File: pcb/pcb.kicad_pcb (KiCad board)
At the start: 2 copper layers, 1 part

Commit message: Finalisation PCB
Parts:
- removed REF**: MODULE_NUCLEO-L432KC, NUCLEO-L432KC:MODULE_NUCLEO-L432KC
- added C1: 1n, Capacitor_THT:CP_Radial_D4.0mm_P1.50mm, F.Cu at (114.3, 119.4)
- added C2: 10u, Capacitor_THT:CP_Radial_D4.0mm_P1.50mm, F.Cu at (74.0, 119.0)
- added C3: 1u, Capacitor_THT:CP_Radial_D4.0mm_P1.50mm, F.Cu at (103.0, 103.0)
- added J1: VIN VBAT, Connector_PinHeader_2.00mm:PinHeader_1x04_P2.00mm_Vertical, F.Cu at (86.0, 80.0)
- added J2: Conn_01x04, Connector_PinHeader_2.00mm:PinHeader_1x04_P2.00mm_Vertical, F.Cu at (59.7, 104.7)
- added J3: AudioJack3, Connector_Audio:Jack_3.5mm_Ledino_KB3SPRS_Horizontal, F.Cu at (101.6, 119.4)
- added J4: Conn_01x04, Connector_PinHeader_2.00mm:PinHeader_1x04_P2.00mm_Vertical, F.Cu at (59.7, 92.7)
- added J5: HX711, Connector_PinHeader_2.00mm:PinHeader_1x04_P2.00mm_Vertical, F.Cu at (114.0, 85.0)
- added J6: Conn_01x04, Connector_PinHeader_2.00mm:PinHeader_1x04_P2.00mm_Vertical, F.Cu at (86.0, 86.0)
- added J7: Conn_01x04, Connector_PinHeader_2.00mm:PinHeader_1x04_P2.00mm_Vertical, F.Cu at (59.7, 81.3)
- added L432KC1: NUCLEO_L432KC, NUCLEO-L432KC:MODULE_NUCLEO-L432KC, F.Cu at (73.7, 85.1)
- added R1: 4.7k, Resistor_THT:R_Axial_DIN0204_L3.6mm_D1.6mm_P5.08mm_Horizontal, F.Cu at (108.0, 110.5)
- added R2: 10k, Resistor_THT:R_Axial_DIN0204_L3.6mm_D1.6mm_P5.08mm_Horizontal, F.Cu at (98.0, 108.0)
- added R3: 10k, Resistor_THT:R_Axial_DIN0204_L3.6mm_D1.6mm_P5.08mm_Horizontal, F.Cu at (101.6, 99.1)
- added U1: LM386, LM386N-4_NOPB:DIP794W45P254L959H508Q8, F.Cu at (113.0, 98.0)
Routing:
- net /+3V3: track 0.00 -> 138.9 mm
- net /+5V: track 0.00 -> 69.4 mm
- net Net-(C1-Pad1): track 0.00 -> 39.3 mm
- net /A2: track 0.00 -> 31.5 mm
- net /A0: track 0.00 -> 29.6 mm
- net Net-(L432KC1-PadNRST): track 0.00 -> 21.6 mm
- net GND: track 0.00 -> 17.3 mm
- net Net-(C1-Pad2): track 0.00 -> 14.4 mm
- net /D4: track 0.00 -> 11.2 mm
- net Net-(C3-Pad2): track 0.00 -> 7.24 mm
- net /D3: track 0.00 -> 6.47 mm
- net /D12: track 0.00 -> 6.45 mm
- net /A7: track 0.00 -> 5.12 mm
- net /A4: track 0.00 -> 4.99 mm
- added copper zone on B.Cu, net GND
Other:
- board outline added: 74 x 73 mm
- board text added: "HX711"

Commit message: Finalisation PCB
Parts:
- added J8: Conn_01x08, Connector_PinHeader_2.00mm:PinHeader_1x08_P2.00mm_Vertical, F.Cu at (122.0, 64.0)
- added R4: 2k, Resistor_THT:R_Axial_DIN0204_L3.6mm_D1.6mm_P5.08mm_Vertical, F.Cu at (153.0, 80.0)
- added R5: 1k, Resistor_THT:R_Axial_DIN0204_L3.6mm_D1.6mm_P5.08mm_Vertical, F.Cu at (148.0, 83.0)
- C1: value 1n -> 1u; footprint Capacitor_THT:CP_Radial_D4.0mm_P1.50mm -> Capacitor_THT:CP_Radial_D5.0mm_P2.00mm
- C2: footprint Capacitor_THT:CP_Radial_D4.0mm_P1.50mm -> Capacitor_THT:CP_Radial_D5.0mm_P2.00mm
- moved C2 103.4 mm to (177.0, 110.0)
- moved J1 67.1 mm to (153.0, 76.0)
- moved C1 62.0 mm to (176.3, 120.4)
- moved C3 62.0 mm to (165.0, 104.0)
- moved J2 62.0 mm to (121.7, 105.7)
- moved J3 62.0 mm to (163.6, 120.4)
- moved J4 62.0 mm to (121.7, 93.7)
- moved J5 62.0 mm to (176.0, 86.0)
- moved J6 62.0 mm to (148.0, 87.0)
- moved J7 62.0 mm to (121.7, 82.3)
- moved L432KC1 62.0 mm to (135.7, 86.1)
- moved R2 62.0 mm to (160.0, 109.0)
- moved R3 62.0 mm to (163.6, 100.1)
- moved U1 62.0 mm to (175.0, 99.0)
- moved R1 62.0 mm to (169.9, 111.5)
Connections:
- J1 pad 1: /A7 -> Net-(J1-Pad1)
- J6 pad 2: Net-(J6-Pad2) -> GND
- L432KC1 pad PA9: Net-(L432KC1-PadPA9) -> /D1
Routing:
- net /+3V3: track 138.9 -> 173.9 mm
- net /+5V: track 69.4 -> 92.3 mm
- net Net-(L432KC1-PadNRST): track 21.6 -> 0.00 mm
- net GND: track 17.3 -> 0.00 mm
- net /D1: track 0.00 -> 11.2 mm
- net Net-(J1-Pad1): track 0.00 -> 4.00 mm
- net /A7: track 5.12 -> 7.69 mm
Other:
- board size 74 x 73 mm -> 72 x 72 mm

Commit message: ...
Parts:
- R4: value 2k -> 1K
- R5: value 1k -> 2k
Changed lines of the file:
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@@
     (pad_to_mask_clearance 0)
     (aux_axis_origin 0 0)
-    (visible_elements FFFFEFFF)
+    (visible_elements FFFFE7FF)
     (pcbplotparams
       (layerselection 0x010fc_ffffffff)
@@
       (effects (font (size 1 1) (thickness 0.15)))
     )
-    (fp_text value 1k (at 2.54 1.92) (layer F.Fab)
+    (fp_text value 2k (at 2.54 1.92) (layer F.Fab)
       (effects (font (size 1 1) (thickness 0.15)))
     )
@@
       (effects (font (size 1 1) (thickness 0.15)))
     )
-    (fp_text value 2k (at 2.54 1.92) (layer F.Fab)
-      (effects (font (size 1 1) (thickness 0.15)))
-    )
+    (fp_text value 1K (at 2.54 1.92) (layer F.Fab)
+      (effects (font (size 1 1) (thickness 0.15)))
+    )

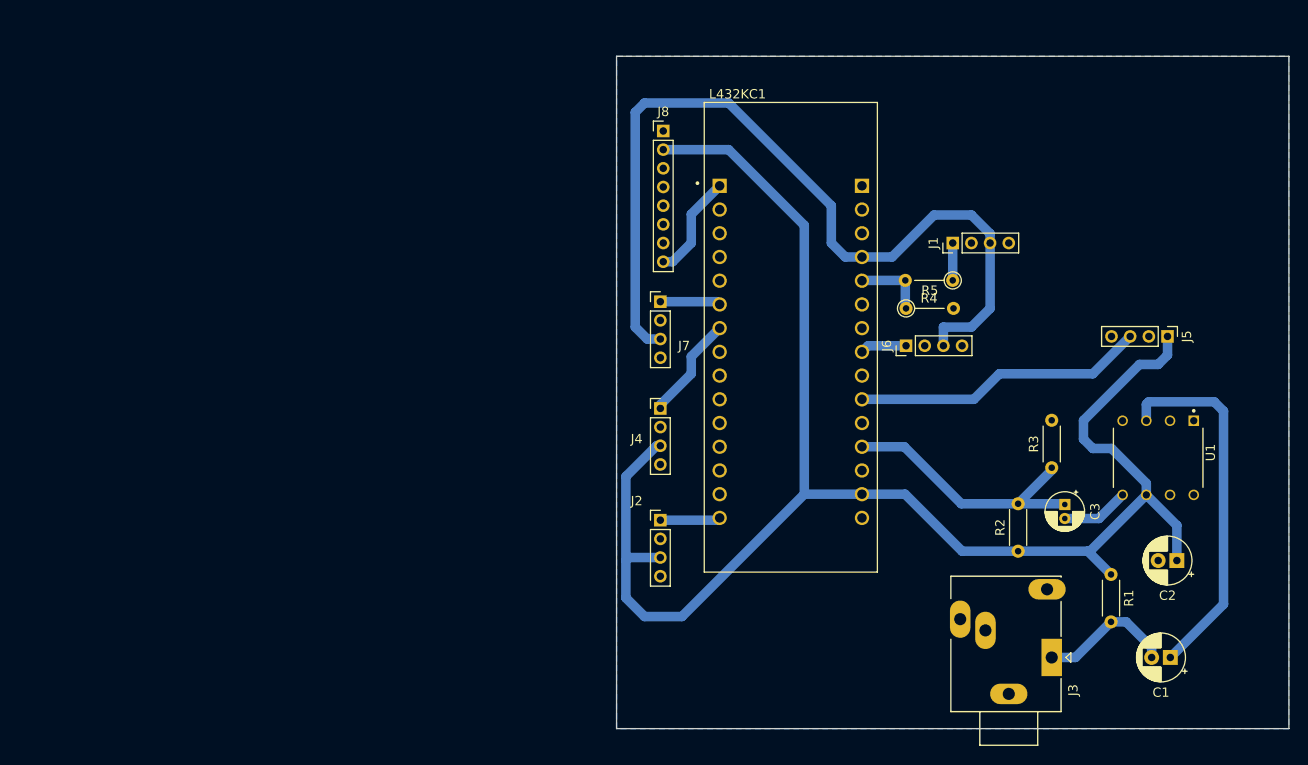
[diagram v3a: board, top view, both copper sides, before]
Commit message: Changement LDO et choix alim
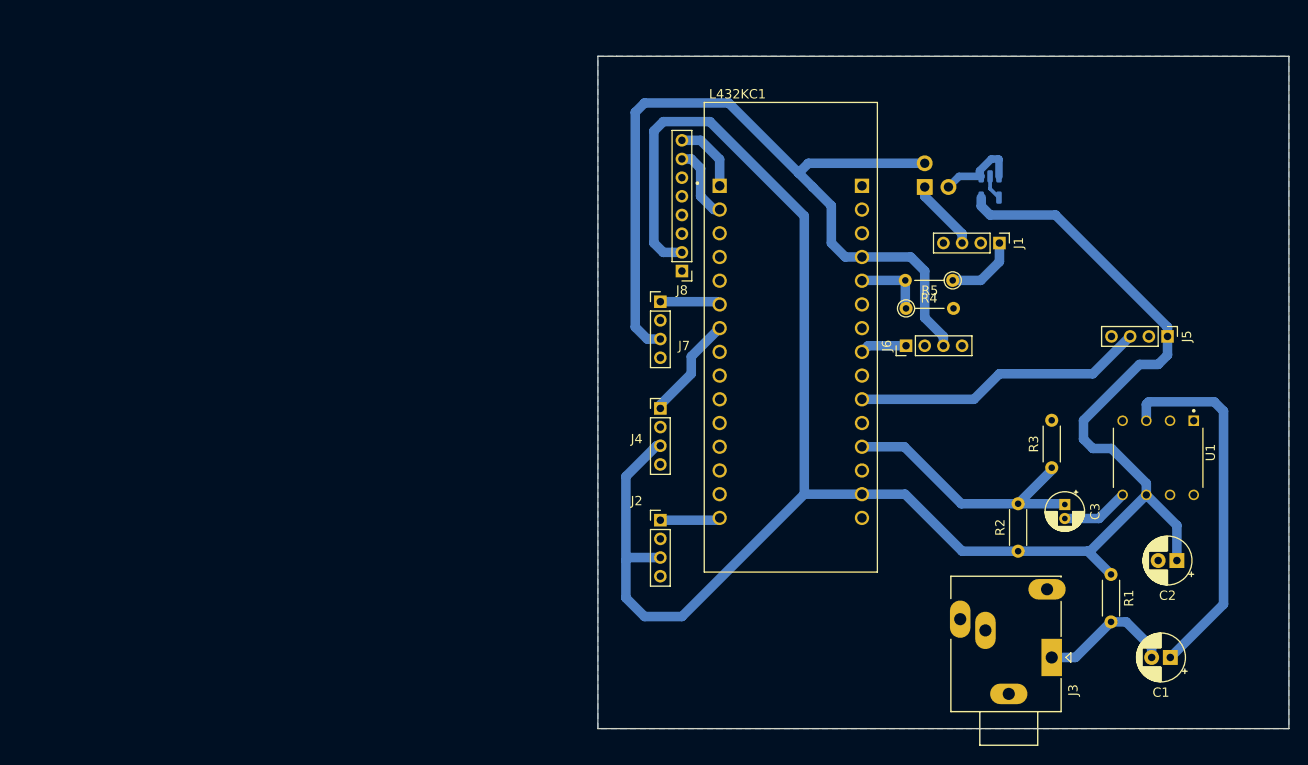
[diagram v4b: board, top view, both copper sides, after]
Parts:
- added SW1: SW_DPDT_x2, Connector_PinHeader_2.54mm:PinHeader_2x02_P2.54mm_Vertical, B.Cu at (150.0, 70.0)
- added U3: TS5205CX533, Package_TO_SOT_SMD:SOT-23-5, B.Cu at (157.0, 70.0)
- moved J8 15.1 mm to (124.0, 79.0), turned to 180 degrees
- moved J1 5.00 mm to (158.0, 76.0), turned to 270 degrees
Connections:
- J1 pad 3: /+5V -> /V_alim
- J7 pad 2: Net-(J7-Pad2) -> GND
- J8 pad 7: Net-(J8-Pad7) -> /D0
- L432KC1 pad PA10: Net-(L432KC1-PadPA10) -> /D0
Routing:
- net /+3V3: track 173.9 -> 219.8 mm
- net Net-(SW1-Pad3): track 0.00 -> 9.02 mm
- net /D0: track 0.00 -> 8.04 mm
- net /V_alim: track 0.00 -> 7.66 mm
- net Net-(J1-Pad1): track 4.00 -> 7.83 mm
- net /D1: track 11.2 -> 7.72 mm
- net GND: track 0.00 -> 2.67 mm
- net /+5V: track 92.3 -> 90.2 mm
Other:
- board size 72 x 72 mm -> 74 x 72 mm

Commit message: Finalisation PCB
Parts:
- added C4: 470p, Capacitor_SMD:C_0805_2012Metric_Pad1.18x1.45mm_HandSolder, B.Cu at (160.0, 68.0)
- added C5: 2.2u, Capacitor_SMD:C_0805_2012Metric_Pad1.18x1.45mm_HandSolder, B.Cu at (157.0, 72.0)
- moved U3 2.24 mm to (156.0, 68.0)
- moved SW1 1.00 mm to (149.0, 70.0)
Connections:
- U3 pad 4: GND -> Net-(C4-Pad1)
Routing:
- net /+3V3: track 219.8 -> 223.9 mm
- net Net-(C4-Pad1): track 0.00 -> 3.09 mm
- net Net-(SW1-Pad3): track 9.02 -> 10.8 mm
- net /+5V: track 90.2 -> 88.9 mm
- net /V_alim: track 7.66 -> 8.66 mm

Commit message: Audio jack a la masse
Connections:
- J3 pad R: Net-(J3-PadR) -> GND

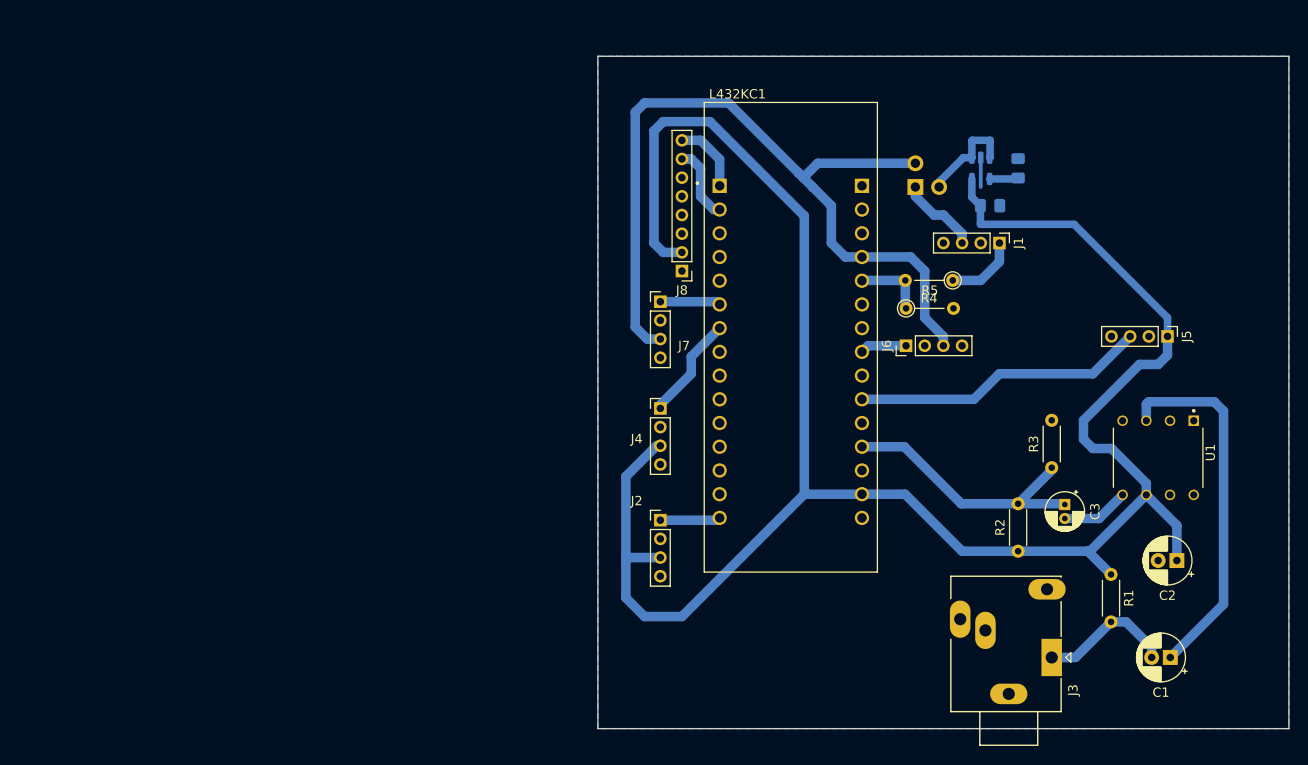
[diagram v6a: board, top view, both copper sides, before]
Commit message: Modification pin HX711
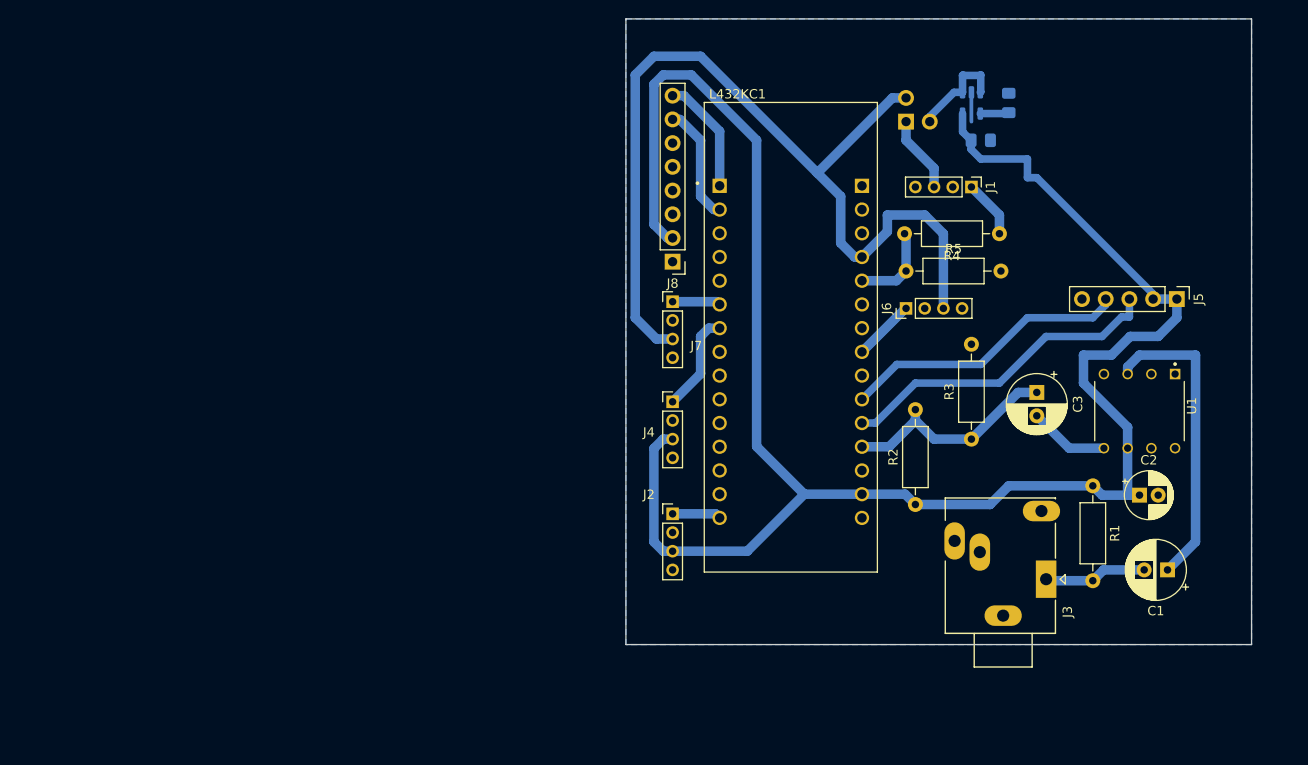
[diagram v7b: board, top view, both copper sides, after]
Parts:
- C1: footprint Capacitor_THT:CP_Radial_D5.0mm_P2.00mm -> Capacitor_THT:CP_Radial_D6.3mm_P2.50mm
- C3: footprint Capacitor_THT:CP_Radial_D4.0mm_P1.50mm -> Capacitor_THT:CP_Radial_D6.3mm_P2.50mm
- J5: value HX711 -> Conn_01x05; footprint Connector_PinHeader_2.00mm:PinHeader_1x04_P2.00mm_Vertical -> Connector_PinHeader_2.54mm:PinHeader_1x05_P2.54mm_Vertical
- J8: footprint Connector_PinHeader_2.00mm:PinHeader_1x08_P2.00mm_Vertical -> Connector_PinHeader_2.54mm:PinHeader_1x08_P2.54mm_Vertical
- R1, R2, R3: footprint Resistor_THT:R_Axial_DIN0204_L3.6mm_D1.6mm_P5.08mm_Horizontal -> Resistor_THT:R_Axial_DIN0207_L6.3mm_D2.5mm_P10.16mm_Horizontal
- R4, R5: footprint Resistor_THT:R_Axial_DIN0204_L3.6mm_D1.6mm_P5.08mm_Vertical -> Resistor_THT:R_Axial_DIN0207_L6.3mm_D2.5mm_P10.16mm_Horizontal
- moved C3 12.4 mm to (162.0, 92.0)
- moved R2 12.1 mm to (149.0, 104.0)
- moved R1 9.69 mm to (168.0, 102.0)
- moved C1 9.38 mm to (176.0, 111.0)
- moved R3 9.13 mm to (155.0, 97.0)
- moved J3 8.40 mm to (163.0, 112.0)
- moved C2 8.06 mm to (173.0, 103.0), turned to 0 degrees
- moved C4 7.07 mm to (159.0, 61.0)
- moved C5 7.07 mm to (156.0, 65.0)
- moved R4 7.07 mm to (158.0, 75.0)
- moved SW1 7.07 mm to (148.0, 63.0)
- moved U3 7.07 mm to (155.0, 61.0)
- moved J1 6.71 mm to (155.0, 70.0)
- moved U1 5.39 mm to (173.0, 94.0)
- moved J5 4.12 mm to (177.0, 82.0)
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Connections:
- J5 pad 2: GND -> /+3V3
- J5 pad 3: /A2 -> /A1
- J5 pad 4: GND -> /A2
- L432KC1 pad PA1: Net-(L432KC1-PadPA1) -> /A1
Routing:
- net /A1: track 0.00 -> 35.3 mm
- net /+3V3: track 223.9 -> 206.1 mm
- net /+5V: track 88.9 -> 101.2 mm
- net Net-(C1-Pad1): track 39.3 -> 32.8 mm
- net /A0: track 29.6 -> 23.9 mm
- net /D1: track 7.72 -> 12.5 mm
- net /D0: track 8.04 -> 12.6 mm
- net Net-(C1-Pad2): track 14.5 -> 11.0 mm
- net /A4: track 4.99 -> 6.65 mm
- net Net-(J1-Pad1): track 7.83 -> 6.24 mm
- net /A7: track 7.69 -> 9.21 mm
- net Net-(C3-Pad2): track 7.24 -> 8.63 mm
- net /D3: track 6.47 -> 5.16 mm
- net /D12: track 6.45 -> 5.22 mm
- net /A2: track 31.5 -> 30.9 mm
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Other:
- board size 74 x 72 mm -> 67 x 67 mm

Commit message: Ajout via
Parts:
- R4: value 1K -> 2.2k
- R5: value 2k -> 3.3k
- moved R3 3.00 mm to (155.0, 100.0)
- moved J6 2.00 mm to (148.0, 85.0)
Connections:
- J2 pad 1: /D12 -> /D10
- J5 pad 3: /A1 -> /DATA
- J5 pad 4: /A2 -> /CLK
- L432KC1 pad PA1: /A1 -> Net-(L432KC1-PadPA1)
- L432KC1 pad PA11: Net-(L432KC1-PadPA11) -> /D10
- L432KC1 pad PA3: /A2 -> Net-(L432KC1-PadPA3)
- L432KC1 pad PA7: Net-(L432KC1-PadPA7) -> /CLK
- L432KC1 pad PB4: /D12 -> /DATA
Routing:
- net /DATA: track 0.00 -> 82.8 mm, vias 0 -> 4
- net /A1: track 35.3 -> 0.00 mm
- net /A2: track 30.9 -> 0.00 mm
- net /CLK: track 0.00 -> 20.7 mm, vias 0 -> 2
- net /+3V3: track 206.1 -> 218.3 mm
- net /D10: track 0.00 -> 6.96 mm
- net /D12: track 5.22 -> 0.00 mm
- net /A0: track 23.9 -> 28.0 mm
- net /+5V: track 101.2 -> 103.9 mm
- net /A4: track 6.65 -> 5.82 mm
